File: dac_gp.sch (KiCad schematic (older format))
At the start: 14 parts

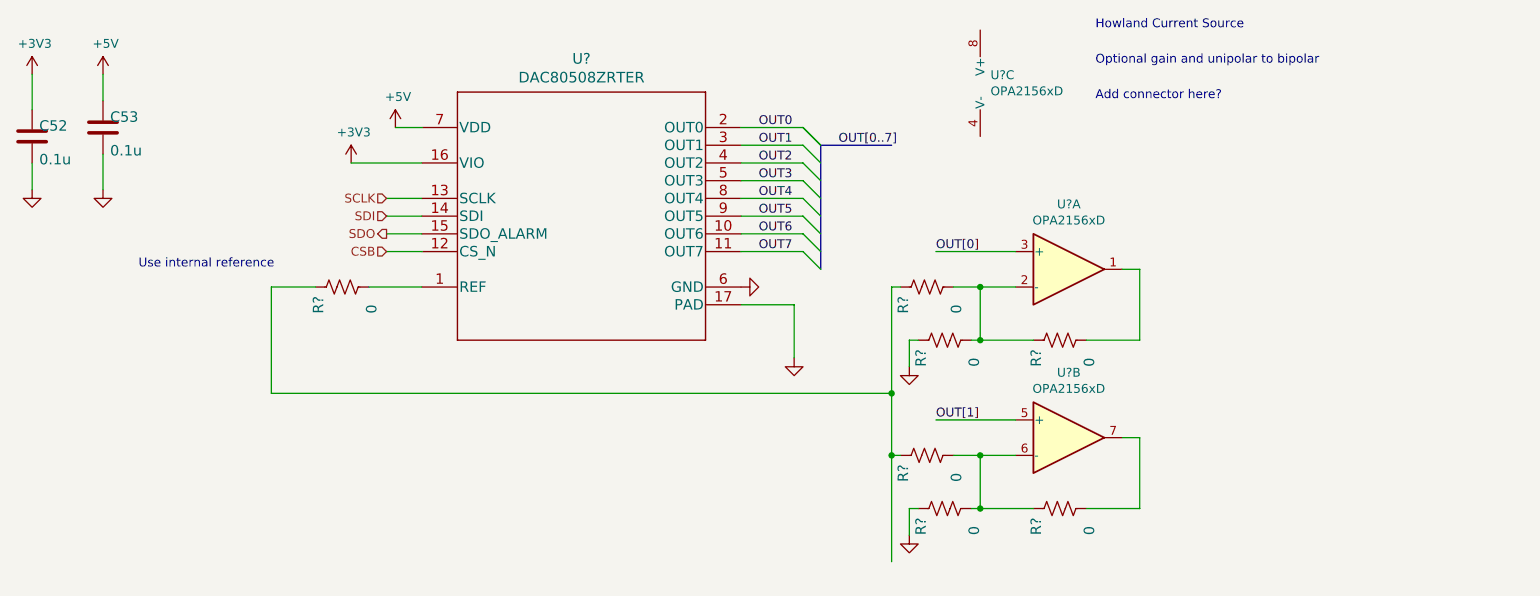
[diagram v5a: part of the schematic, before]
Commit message: updates to the gp DAC
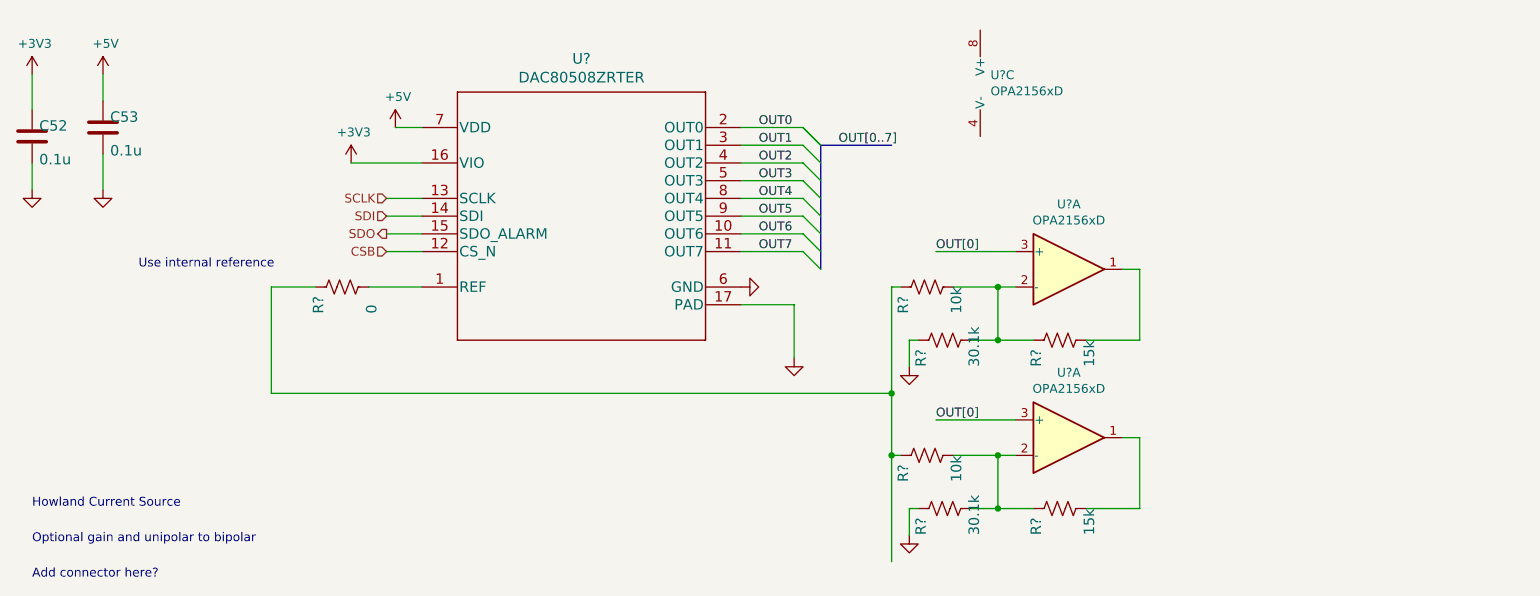
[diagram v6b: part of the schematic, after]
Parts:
- removed R? (x3): 0, Resistor_SMD:R_0603_1608Metric, symbol Device:R_US
- removed U?: OPA2156xD, Package_SO:SOIC-8_3.9x4.9mm_P1.27mm, symbol Amplifier_Operational:OPA2156xD
- added R?: 10k, Resistor_SMD:R_0603_1608Metric, symbol Device:R_US
- added R?: 30.1k, Resistor_SMD:R_0603_1608Metric, symbol Device:R_US
- added R?: 15k, Resistor_SMD:R_0603_1608Metric, symbol Device:R_US
- added U?: OPA2156xD, Package_SO:SOIC-8_3.9x4.9mm_P1.27mm, symbol Amplifier_Operational:OPA2156xD
- R?: value 0 -> 10k; Manf# (none) -> RC0603FR-0710kL
- R?: value 0 -> 30.1k; Manf# (none) -> RC0603FR-0730k1L
- R?: value 0 -> 15k; Manf# (none) -> RC0603FR-0715kL
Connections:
- net GND: now also R?.1
- net OUT[0]: now also U?.3 (+)
- net at R?.1, R?.1: now also R?.1
- new net: R?.2, U?.1
- new net: R?.1, R?.2, R?.2, U?.2 (-)
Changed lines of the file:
@@
 $Descr User 12505 8268
 encoding utf-8
-Sheet 3 8
+Sheet 3 9
 Title ""
 Date ""
@@
 Text Label 5200 1300 0    50   ~ 0
 OUT[0..7]
-Text Notes 6650 650  0    50   ~ 0
+Text Notes 650  3350 0    50   ~ 0
 Howland Current Source  (needs to MUX to any DAC HDMI signal)
-Text Notes 6650 850  0    50   ~ 0
+Text Notes 650  3550 0    50   ~ 0
 Optional gain and unipolar to bipolar
-Text Notes 6650 1050 0    50   ~ 0
+Text Notes 650  3750 0    50   ~ 0
 Add connector here?
 $Comp
@@
 AR Path="/6095BD4C/60B473F3" Ref="R?"  Part="1"
 F 0 "R?" H 5550 2200 59  0000 L BNN
-F 1 "0" H 5550 1900 59  0000 L BNN
+F 1 "10k" H 5550 1900 59  0000 L BNN
 F 2 "Resistor_SMD:R_0603_1608Metric" H 5700 2100 50  0001 C CNN
 F 3 "" H 5700 2100 50  0001 C CNN
+F 4 "RC0603FR-0710kL" H 5700 2100 50  0001 C CNN "Manf#"
 	1    5700 2100
 	0    -1   -1   0
-$EndComp
-$Comp
-L Amplifier_Operational:OPA2156xD U?
-U 2 1 60B47D89
-P 6500 2950
-F 0 "U?" H 6500 3317 50  0000 C CNN
-F 1 "OPA2156xD" H 6500 3226 50  0000 C CNN
-F 2 "Package_SO:SOIC-8_3.9x4.9mm_P1.27mm" H 6600 2950 50  0001 C CNN
-F 3 "https://www.ti.com/lit/ds/symlink/opa2156.pdf" H 6750 3100 50  0001 C CNN
-	2    6500 2950
-	1    0    0    -1
 $EndComp
 $Comp
@@
 AR Path="/6095BD4C/60B4B5D2" Ref="R?"  Part="1"
 F 0 "R?" H 5650 2500 59  0000 L BNN
-F 1 "0" H 5650 2200 59  0000 L BNN
+F 1 "30.1k" H 5650 2200 59  0000 L BNN
 F 2 "Resistor_SMD:R_0603_1608Metric" H 5800 2400 50  0001 C CNN
 F 3 "" H 5800 2400 50  0001 C CNN
+F 4 "RC0603FR-0730k1L" H 5800 2400 50  0001 C CNN "Manf#"
 	1    5800 2400
 	0    -1   -1   0
@@
 	5600 2400 5650 2400
 Wire Wire Line
-	6000 2400 6000 2100
-Wire Wire Line
-	6200 2100 6000 2100
-Connection ~ 6000 2100
+	6100 2400 6100 2100
+Wire Wire Line
+	6200 2100 6100 2100
+Connection ~ 6100 2100
 $Comp
 L Device:R_US R?
@@
 AR Path="/6095BD4C/60B4DB38" Ref="R?"  Part="1"
 F 0 "R?" H 6300 2500 59  0000 L BNN
-F 1 "0" H 6300 2200 59  0000 L BNN
+F 1 "15k" H 6300 2200 59  0000 L BNN
 F 2 "Resistor_SMD:R_0603_1608Metric" H 6450 2400 50  0001 C CNN
 F 3 "" H 6450 2400 50  0001 C CNN
+F 4 "RC0603FR-0715kL" H 6450 2400 50  0001 C CNN "Manf#"
 	1    6450 2400
 	0    -1   -1   0
 $EndComp
 Wire Wire Line
-	6300 2400 6000 2400
-Connection ~ 6000 2400
+	6300 2400 6100 2400
+Connection ~ 6100 2400
 Wire Wire Line
 	6600 2400 6900 2400
@@
 OUT[0]
 Wire Wire Line
-	6000 2100 5850 2100
-Wire Wire Line
-	5950 2400 6000 2400
-$Comp
-L Device:R_US R?
-U 1 1 60B54334
-P 5700 3050
-AR Path="/6095A38A/60B54334" Ref="R?"  Part="1"
-AR Path="/6095BD4C/60B54334" Ref="R?"  Part="1"
-F 0 "R?" H 5550 3150 59  0000 L BNN
-F 1 "0" H 5550 2850 59  0000 L BNN
-F 2 "Resistor_SMD:R_0603_1608Metric" H 5700 3050 50  0001 C CNN
-F 3 "" H 5700 3050 50  0001 C CNN
-	1    5700 3050
-	0    -1   -1   0
-$EndComp
+	6100 2100 5850 2100
+Wire Wire Line
+	5950 2400 6100 2400
 Wire Wire Line
 	5500 3050 5550 3050
 Wire Wire Line
 	5500 3050 5500 3650
-$Comp
-L Device:R_US R?
-U 1 1 60B5433C
-P 5800 3350
-AR Path="/6095A38A/60B5433C" Ref="R?"  Part="1"
-AR Path="/6095BD4C/60B5433C" Ref="R?"  Part="1"
-F 0 "R?" H 5650 3450 59  0000 L BNN
-F 1 "0" H 5650 3150 59  0000 L BNN
-F 2 "Resistor_SMD:R_0603_1608Metric" H 5800 3350 50  0001 C CNN
-F 3 "" H 5800 3350 50  0001 C CNN
-	1    5800 3350
-	0    -1   -1   0
-$EndComp
-$Comp
-L power:GND #GND?
-U 1 1 60B54342
-P 5600 3500
-F 0 "#GND?" H 5600 3500 50  0001 C CNN
-F 1 "GND" H 5500 3400 59  0001 L BNN
-F 2 "" H 5600 3500 50  0001 C CNN
-F 3 "" H 5600 3500 50  0001 C CNN
-	1    5600 3500
-	1    0    0    -1
-$EndComp
-Wire Wire Line
-	5600 3500 5600 3350
-Wire Wire Line
-	5600 3350 5650 3350
-Wire Wire Line
-	6000 3350 6000 3050
-Wire Wire Line
-	6200 3050 6000 3050
-Connection ~ 6000 3050
-Wire Wire Line
-	6300 3350 6000 3350
-Connection ~ 6000 3350
-Wire Wire Line
-	6000 3050 5850 3050
-Wire Wire Line
-	5950 3350 6000 3350
-Wire Wire Line
-	6200 2850 5750 2850
 Wire Wire Line
 	5500 2700 5500 3050
 Connection ~ 5500 2700
 Connection ~ 5500 3050
-$Comp
-L Device:R_US R?
-U 1 1 60B56A38
-P 6450 3350
-AR Path="/6095A38A/60B56A38" Ref="R?"  Part="1"
-AR Path="/6095BD4C/60B56A38" Ref="R?"  Part="1"
-F 0 "R?" H 6300 3450 59  0000 L BNN
-F 1 "0" H 6300 3150 59  0000 L BNN
-F 2 "Resistor_SMD:R_0603_1608Metric" H 6450 3350 50  0001 C CNN
-F 3 "" H 6450 3350 50  0001 C CNN
-	1    6450 3350
-	0    -1   -1   0
-$EndComp
-Wire Wire Line
-	6600 3350 6900 3350
-Wire Wire Line
-	6900 3350 6900 2950
-Wire Wire Line
-	6900 2950 6800 2950
-Text Label 5750 2850 0    50   ~ 0
-OUT[1]
 $Comp
 L covg-kicad:TMUX6136PWR U?
@@
 Wire Wire Line
 	2000 2700 5500 2700
+$Comp
+L Amplifier_Operational:OPA2156xD U?
+U 1 1 60BA9741
+P 6500 2950
+F 0 "U?" H 6500 3317 50  0000 C CNN
+F 1 "OPA2156xD" H 6500 3226 50  0000 C CNN
+F 2 "Package_SO:SOIC-8_3.9x4.9mm_P1.27mm" H 6600 2950 50  0001 C CNN
+F 3 "https://www.ti.com/lit/ds/symlink/opa2156.pdf" H 6750 3100 50  0001 C CNN
+	1    6500 2950
+	1    0    0    -1
+$EndComp
+$Comp
+L Device:R_US R?
+U 1 1 60BA9748
+P 5700 3050
+AR Path="/6095A38A/60BA9748" Ref="R?"  Part="1"
+AR Path="/6095BD4C/60BA9748" Ref="R?"  Part="1"
+F 0 "R?" H 5550 3150 59  0000 L BNN
+F 1 "10k" H 5550 2850 59  0000 L BNN
+F 2 "Resistor_SMD:R_0603_1608Metric" H 5700 3050 50  0001 C CNN
+F 3 "" H 5700 3050 50  0001 C CNN
+F 4 "RC0603FR-0710kL" H 5700 3050 50  0001 C CNN "Manf#"
+	1    5700 3050
+	0    -1   -1   0
+$EndComp
+$Comp
+L Device:R_US R?
+U 1 1 60BA9751
+P 5800 3350
+AR Path="/6095A38A/60BA9751" Ref="R?"  Part="1"
+AR Path="/6095BD4C/60BA9751" Ref="R?"  Part="1"
+F 0 "R?" H 5650 3450 59  0000 L BNN
+F 1 "30.1k" H 5650 3150 59  0000 L BNN
+F 2 "Resistor_SMD:R_0603_1608Metric" H 5800 3350 50  0001 C CNN
+F 3 "" H 5800 3350 50  0001 C CNN
+F 4 "RC0603FR-0730k1L" H 5800 3350 50  0001 C CNN "Manf#"
+	1    5800 3350
+	0    -1   -1   0
+$EndComp
+$Comp
+L power:GND #GND?
+U 1 1 60BA9757
+P 5600 3500
+F 0 "#GND?" H 5600 3500 50  0001 C CNN
+F 1 "GND" H 5500 3400 59  0001 L BNN
+F 2 "" H 5600 3500 50  0001 C CNN
+F 3 "" H 5600 3500 50  0001 C CNN
+	1    5600 3500
+	1    0    0    -1
+$EndComp
+Wire Wire Line
+	5600 3500 5600 3350
+Wire Wire Line
+	5600 3350 5650 3350
+Wire Wire Line
+	6100 3350 6100 3050
+Wire Wire Line
+	6200 3050 6100 3050
+Connection ~ 6100 3050
+$Comp
+L Device:R_US R?
+U 1 1 60BA9763
+P 6450 3350
+AR Path="/6095A38A/60BA9763" Ref="R?"  Part="1"
+AR Path="/6095BD4C/60BA9763" Ref="R?"  Part="1"
+F 0 "R?" H 6300 3450 59  0000 L BNN
+F 1 "15k" H 6300 3150 59  0000 L BNN
+F 2 "Resistor_SMD:R_0603_1608Metric" H 6450 3350 50  0001 C CNN
+F 3 "" H 6450 3350 50  0001 C CNN
+F 4 "RC0603FR-0715kL" H 6450 3350 50  0001 C CNN "Manf#"
+	1    6450 3350
+	0    -1   -1   0
+$EndComp
+Wire Wire Line
+	6300 3350 6100 3350
+Connection ~ 6100 3350
+Wire Wire Line
+	6600 3350 6900 3350
+Wire Wire Line
+	6900 3350 6900 2950
+Wire Wire Line
+	6900 2950 6800 2950
+Wire Wire Line
+	6200 2850 5750 2850
+Text Label 5750 2850 0    50   ~ 0
+OUT[0]
+Wire Wire Line
+	6100 3050 5850 3050
+Wire Wire Line
+	5950 3350 6100 3350
 Wire Bus Line
 	5100 1300 5100 2000

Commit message: updates to gp_dac
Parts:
- added R12, R13, R? (x4): 15k, Resistor_SMD:R_0603_1608Metric, symbol Device:R_US
- added R4, R5, R? (x4): 10k, Resistor_SMD:R_0603_1608Metric, symbol Device:R_US
- added R8, R9, R? (x4): 30.1k, Resistor_SMD:R_0603_1608Metric, symbol Device:R_US
- added unit 3 of U3
- added U4, U6, U? (x6): OPA2156xD, Package_SO:SOIC-8_3.9x4.9mm_P1.27mm, symbol Amplifier_Operational:OPA2156xD
- added U9: TMUX6136PWR, PW16_TEX, symbol covg-kicad:TMUX6136PWR
- gave numbers to parts that had none: 11
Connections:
- net labels added: +15V, -15V, BP_OUT[4..7], DAC_CAL[0..3], DAC_CAL[0], DAC_CAL[1], DAC_CAL[2], DAC_CAL[3], IPUMP_SDOWN, ISEL[0..3], ISEL[0], ISEL[1], ISEL[2], ISEL[3], OUT[1], OUT[2], OUT[3], OUT[4], OUT[5], OUT[6], OUT[7]
- wire segments 51 -> 179
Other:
- note added: "0 ==> B to D out\n1 ==> A to D out"
- note removed: "Add connector here?"
- note removed: "Howland Current Source (needs to MUX to any DAC HDMI signal)"
- note removed: "Optional gain and unipolar to bipolar"
- moved on the sheet: R1, U1, U2C

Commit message: updates to gp ADC
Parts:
- added C? (x8): 0.1u, Capacitor_SMD:C_0603_1608Metric, symbol Device:C
- C52, C53: Manf# (none) -> CC0603MRX7R8BB104
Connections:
- wire segments 179 -> 194
